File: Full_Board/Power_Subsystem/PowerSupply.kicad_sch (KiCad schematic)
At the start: 20 parts, among them IC4 LM2576HVS-5.0_NOPB, J7 KLDHCX-8-0202-A, U1 LM2576SX-3.3-NOPB

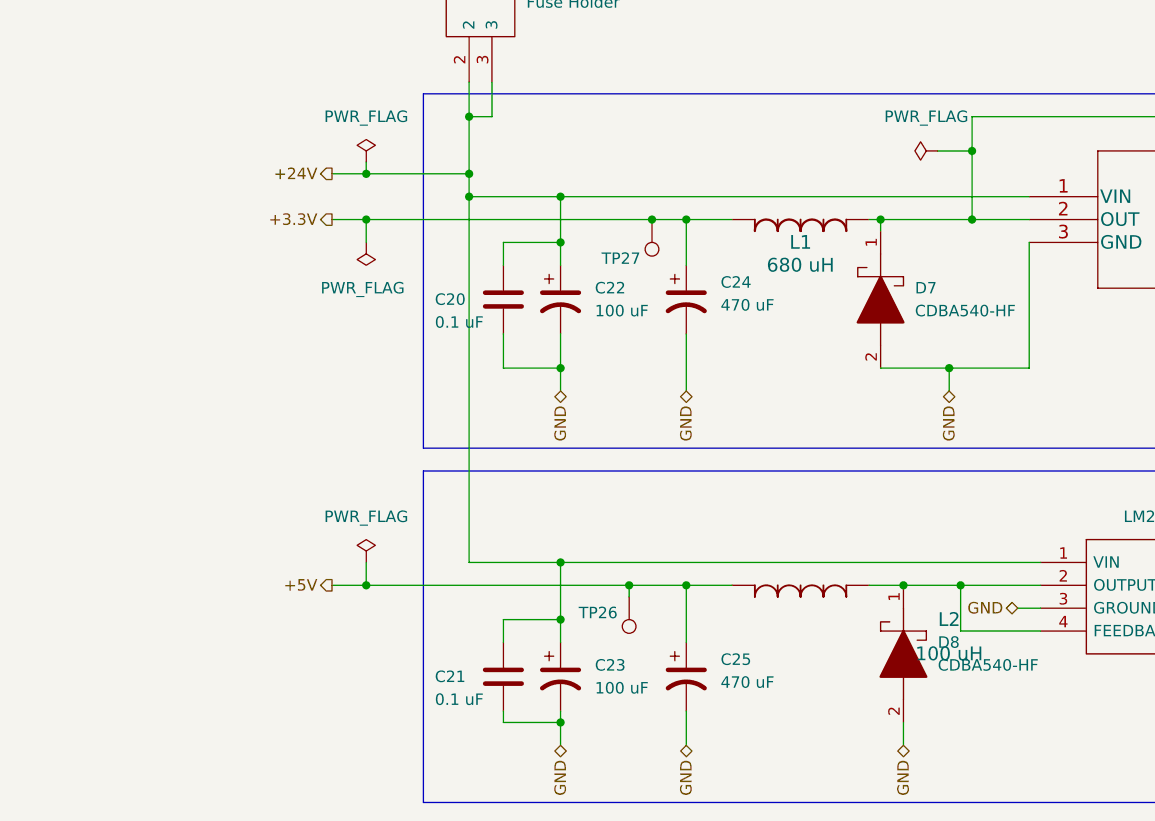
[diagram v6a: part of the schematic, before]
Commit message: Added jumpers to the 3.3 and 5V lines
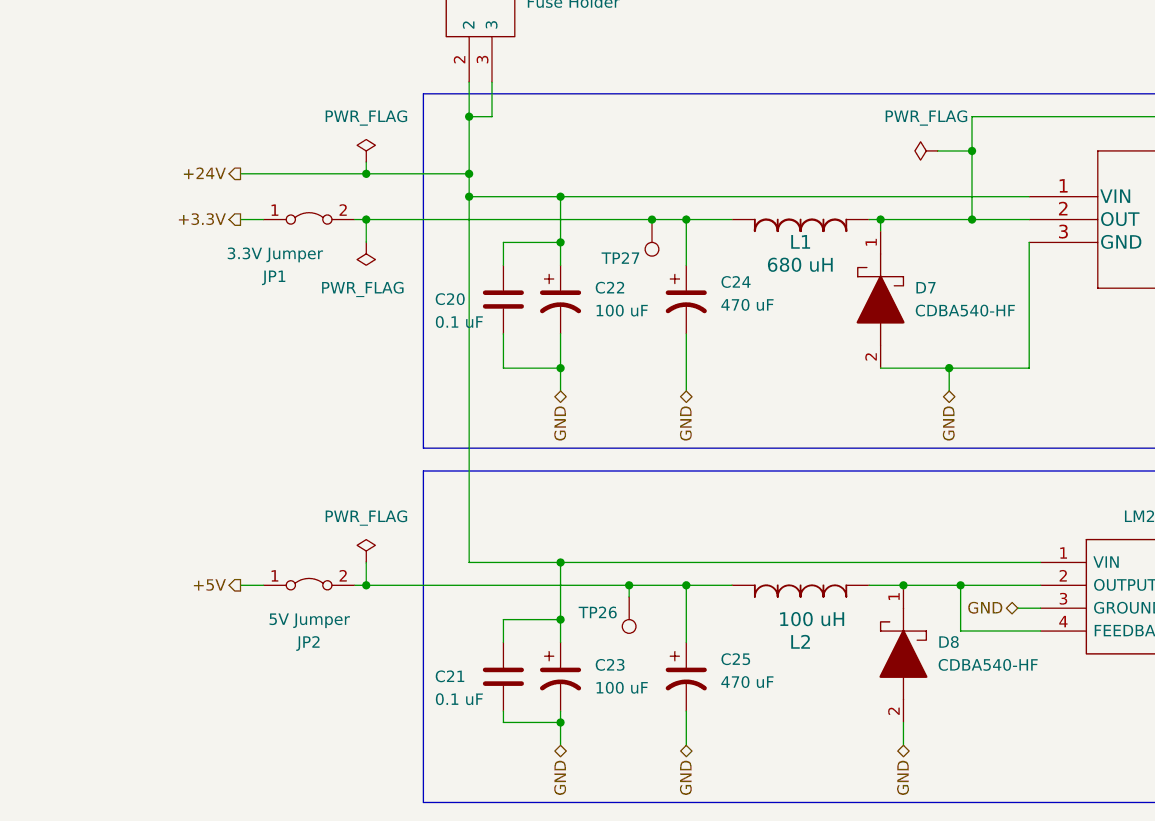
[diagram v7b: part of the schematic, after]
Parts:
- added JP1: 3.3V Jumper, TestPoint:TestPoint_2Pads_Pitch2.54mm_Drill0.8mm, symbol Jumper:Jumper_2_Bridged
- added JP2: 5V Jumper, TestPoint:TestPoint_2Pads_Pitch2.54mm_Drill0.8mm, symbol Jumper:Jumper_2_Bridged
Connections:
- net +3.3V: now also JP1.1 (A); no longer C24.1, L1.1, TP27.1
- net +5V: now also JP2.1 (A); no longer C25.1, L2.1, TP26.1
- new net: C25.1, JP2.2 (B), L2.1, TP26.1
- new net: C24.1, JP1.2 (B), L1.1, TP27.1
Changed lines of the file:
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@@
   (junction (at 134.62 135.89) (diameter 0) (color 0 0 0 0)
   )
+  (junction (at 124.46 46.99) (diameter 0) (color 0 0 0 0)
+  )
+  (junction (at 170.18 111.76) (diameter 0) (color 0 0 0 0)
+  )
+  (junction (at 165.1 135.89) (diameter 0) (color 0 0 0 0)
+  )
+  (junction (at 105.41 95.25) (diameter 0) (color 0 0 0 0)
+  )
+  (junction (at 127 111.76) (diameter 0) (color 0 0 0 0)
+  )
+  (junction (at 127 139.7) (diameter 0) (color 0 0 0 0)
+  )
+  (junction (at 224.79 138.43) (diameter 0) (color 0 0 0 0)
+  )
   (junction (at 105.41 135.89) (diameter 0) (color 0 0 0 0)
   )
-  (junction (at 124.46 46.99) (diameter 0) (color 0 0 0 0)
-  )
-  (junction (at 170.18 111.76) (diameter 0) (color 0 0 0 0)
-  )
-  (junction (at 165.1 135.89) (diameter 0) (color 0 0 0 0)
-  )
-  (junction (at 127 111.76) (diameter 0) (color 0 0 0 0)
-  )
-  (junction (at 127 139.7) (diameter 0) (color 0 0 0 0)
-  )
-  (junction (at 224.79 138.43) (diameter 0) (color 0 0 0 0)
-  )
   (junction (at 140.97 135.89) (diameter 0) (color 0 0 0 0)
   )
   (junction (at 129.54 46.99) (diameter 0) (color 0 0 0 0)
-  )
-  (junction (at 105.41 95.25) (diameter 0) (color 0 0 0 0)
   )
   (junction (at 224.79 135.89) (diameter 0) (color 0 0 0 0)
@@
     (stroke (width 0) (type default) (color 0 0 0 0))
   )
+  (wire (pts (xy 91.44 135.89) (xy 93.98 135.89))
+    (stroke (width 0) (type default) (color 0 0 0 0))
+  )
   (wire (pts (xy 172.72 83.82) (xy 172.72 87.63))
     (stroke (width 0) (type default) (color 0 0 0 0))
@@
     (stroke (width 0) (type default) (color 0 0 0 0))
   )
-  (wire (pts (xy 101.6 90.17) (xy 105.41 90.17))
+  (wire (pts (xy 91.44 90.17) (xy 105.41 90.17))
     (stroke (width 0) (type default) (color 0 0 0 0))
   )
@@
     (stroke (width 0) (type default) (color 0 0 0 0))
   )
+  (wire (pts (xy 104.14 95.25) (xy 105.41 95.25))
+    (stroke (width 0) (type default) (color 0 0 0 0))
+  )
   (wire (pts (xy 127 139.7) (xy 127 142.24))
     (stroke (width 0) (type default) (color 0 0 0 0))
@@
     (stroke (width 0) (type default) (color 0 0 0 0))
   )
-  (wire (pts (xy 101.6 135.89) (xy 105.41 135.89))
-    (stroke (width 0) (type default) (color 0 0 0 0))
-  )
   (wire (pts (xy 218.44 135.89) (xy 224.79 135.89))
     (stroke (width 0) (type default) (color 0 0 0 0))
@@
     (stroke (width 0) (type default) (color 0 0 0 0))
   )
-  (wire (pts (xy 101.6 95.25) (xy 105.41 95.25))
-    (stroke (width 0) (type default) (color 0 0 0 0))
-  )
   (wire (pts (xy 120.65 97.79) (xy 127 97.79))
     (stroke (width 0) (type default) (color 0 0 0 0))
@@
     (stroke (width 0) (type default) (color 0 0 0 0))
   )
+  (wire (pts (xy 104.14 135.89) (xy 105.41 135.89))
+    (stroke (width 0) (type default) (color 0 0 0 0))
+  )
   (wire (pts (xy 127 107.95) (xy 127 111.76))
     (stroke (width 0) (type default) (color 0 0 0 0))
@@
   )
   (wire (pts (xy 119.38 44.45) (xy 127 44.45))
+    (stroke (width 0) (type default) (color 0 0 0 0))
+  )
+  (wire (pts (xy 91.44 95.25) (xy 93.98 95.25))
     (stroke (width 0) (type default) (color 0 0 0 0))
   )
@@
     (effects (font (size 1.27 1.27)) (justify right))
   )
-  (hierarchical_label "+3.3V" (shape output) (at 101.6 95.25 180)
+  (hierarchical_label "+3.3V" (shape output) (at 91.44 95.25 180)
     (effects (font (size 1.27 1.27)) (justify right))
   )
@@
     (effects (font (size 1.27 1.27)) (justify right))
   )
-  (hierarchical_label "+24V" (shape output) (at 101.6 90.17 180)
+  (hierarchical_label "+24V" (shape output) (at 91.44 90.17 180)
     (effects (font (size 1.27 1.27)) (justify right))
   )
@@
     (effects (font (size 1.27 1.27)) (justify right))
   )
-  (hierarchical_label "+5V" (shape output) (at 101.6 135.89 180)
+  (hierarchical_label "+5V" (shape output) (at 91.44 135.89 180)
     (effects (font (size 1.27 1.27)) (justify right))
   )
@@
     (pin "2")
   )
+  (symbol (lib_id "Jumper:Jumper_2_Bridged") (at 99.06 135.89 0) (unit 1)
+    (in_bom yes) (on_board yes)
+    (property "Reference" "JP2" (id 0) (at 99.06 142.24 0))
+    (property "Value" "5V Jumper" (id 1) (at 99.06 139.7 0))
+    (property "Footprint" "TestPoint:TestPoint_2Pads_Pitch2.54mm_Drill0.8mm" (id 2) (at 99.06 135.89 0)
+      (effects (font (size 1.27 1.27)) hide)
+    )
+    (property "Datasheet" "https://app.adam-tech.com/products/download/data_sheet/201605/ph1-xx-ua-data-sheet.pdf" (id 3) (at 99.06 135.89 0)
+      (effects (font (size 1.27 1.27)) hide)
+    )
+    (property "Manufacturers Part Number" "PH1-02-UA" (id 4) (at 99.06 135.89 0)
+      (effects (font (size 1.27 1.27)) hide)
+    )
+    (property "Digikey Part Number" "2057-PH1-02-UA-ND" (id 5) (at 99.06 135.89 0)
+      (effects (font (size 1.27 1.27)) hide)
+    )
+    (property "Mouser Part Number" "" (id 6) (at 99.06 135.89 0)
+      (effects (font (size 1.27 1.27)) hide)
+    )
+    (property "Digikey Link" "https://www.digikey.com/en/products/detail/adam-tech/PH1-02-UA/9830266" (id 7) (at 99.06 135.89 0)
+      (effects (font (size 1.27 1.27)) hide)
+    )
+    (property "Mouser Link" "" (id 8) (at 99.06 135.89 0)
+      (effects (font (size 1.27 1.27)) hide)
+    )
+    (pin "1")
+    (pin "2")
+  )
   (symbol (lib_id "CDBA540-HF:CDBA540-HF") (at 162.56 93.98 270) (unit 1)
     (in_bom yes) (on_board yes) (fields_autoplaced)
@@
     (pin "2")
   )
+  (symbol (lib_id "Jumper:Jumper_2_Bridged") (at 99.06 95.25 0) (unit 1)
+    (in_bom yes) (on_board yes)
+    (property "Reference" "JP1" (id 0) (at 95.25 101.6 0))
+    (property "Value" "3.3V Jumper" (id 1) (at 95.25 99.06 0))
+    (property "Footprint" "TestPoint:TestPoint_2Pads_Pitch2.54mm_Drill0.8mm" (id 2) (at 99.06 95.25 0)
+      (effects (font (size 1.27 1.27)) hide)
+    )
+    (property "Datasheet" "https://app.adam-tech.com/products/download/data_sheet/201605/ph1-xx-ua-data-sheet.pdf" (id 3) (at 99.06 95.25 0)
+      (effects (font (size 1.27 1.27)) hide)
+    )
+    (property "Manufacturers Part Number" "PH1-02-UA" (id 4) (at 99.06 95.25 0)
+      (effects (font (size 1.27 1.27)) hide)
+    )
+    (property "Digikey Part Number" "2057-PH1-02-UA-ND" (id 5) (at 99.06 95.25 0)
+      (effects (font (size 1.27 1.27)) hide)
+    )
+    (property "Mouser Part Number" "" (id 6) (at 99.06 95.25 0)
+      (effects (font (size 1.27 1.27)) hide)
+    )
+    (property "Digikey Link" "https://www.digikey.com/en/products/detail/adam-tech/PH1-02-UA/9830266" (id 7) (at 99.06 95.25 0)
+      (effects (font (size 1.27 1.27)) hide)
+    )
+    (property "Mouser Link" "" (id 8) (at 99.06 95.25 0)
+      (effects (font (size 1.27 1.27)) hide)
+    )
+    (pin "1")
+    (pin "2")
+  )
   (symbol (lib_id "Connector:TestPoint") (at 134.62 137.16 180) (unit 1)
     (in_bom yes) (on_board yes)
@@
   (symbol (lib_id "PA4344-104NLT:PA4344.104NLT") (at 161.29 135.89 180) (unit 1)
     (in_bom yes) (on_board yes)
-    (property "Reference" "L2" (id 0) (at 170.18 139.7 0)
+    (property "Reference" "L2" (id 0) (at 153.67 142.24 0)
       (effects (font (size 1.524 1.524)))
     )
-    (property "Value" "100 uH" (id 1) (at 170.18 143.51 0)
+    (property "Value" "100 uH" (id 1) (at 154.94 139.7 0)
       (effects (font (size 1.524 1.524)))
     )
